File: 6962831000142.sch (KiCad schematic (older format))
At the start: 75 parts, among them J1 1042490810, J10 A2, J11 B1, J12 B2, J13 C1, J14 C2, J15 D1, J16 D2, J17 SolderPoint +, J18 SolderPoint -, J19 FastenerDrillingGNDREF, J20 FastenerDrilling, J8 1909763-1, J9 A1, Q1 SI2323DS, SW1 SW_Reed_Opener, U1 CC2640R2FRSMT, U2 ADP160AUJZ-2.3-R7, U3 CMKT5087TR, U4 CMKT5087TR, U5 CMKT5087TR, U6 PS09, Y1 TSX-322524.0000MF15X-AC3, Y2 32.768kHz, Y3 24 MHz

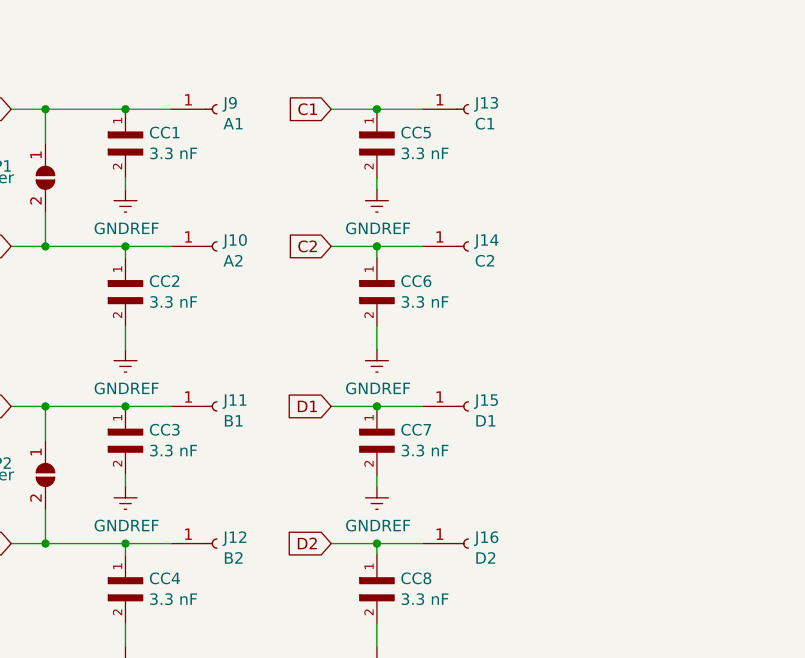
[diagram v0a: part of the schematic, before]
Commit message: se colocaron dos pads soldables
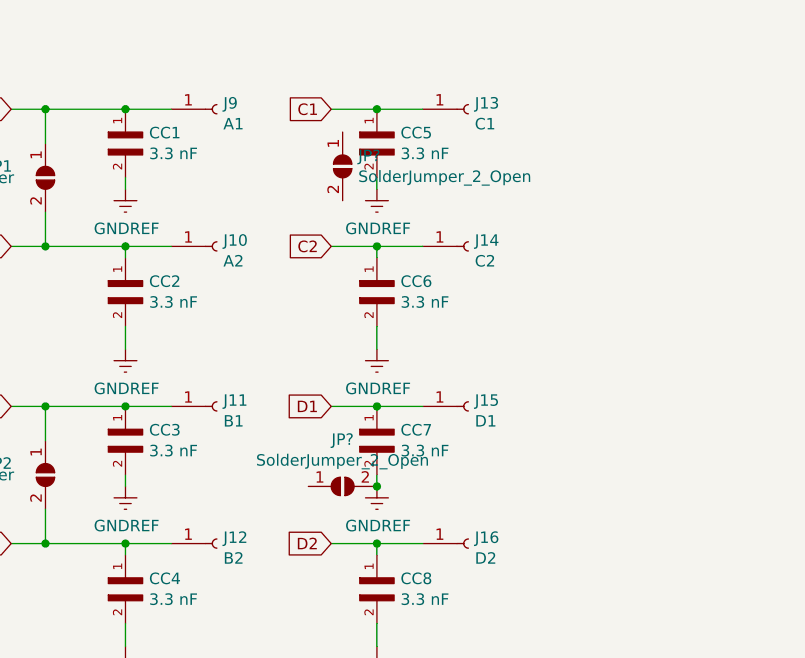
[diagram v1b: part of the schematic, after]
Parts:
- added JP? (x2): SolderJumper_2_Open, symbol Jumper:SolderJumper_2_Open
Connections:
- net GNDREF: now also JP?.2 (B)
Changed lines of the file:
@@
 Wire Wire Line
 	12700 3500 13050 3500
+$Comp
+L Jumper:SolderJumper_2_Open JP?
+U 1 1 5F74EED2
+P 14000 1850
+F 0 "JP?" V 13954 1918 50  0000 L CNN
+F 1 "SolderJumper_2_Open" V 14045 1918 50  0000 L CNN
+F 2 "" H 14000 1850 50  0001 C CNN
+F 3 "~" H 14000 1850 50  0001 C CNN
+	1    14000 1850
+	0    1    1    0
+$EndComp
+$Comp
+L Jumper:SolderJumper_2_Open JP?
+U 1 1 5F74F512
+P 14000 3250
+F 0 "JP?" H 14000 3455 50  0000 C CNN
+F 1 "SolderJumper_2_Open" H 14000 3364 50  0000 C CNN
+F 2 "" H 14000 3250 50  0001 C CNN
+F 3 "~" H 14000 3250 50  0001 C CNN
+	1    14000 3250
+	1    0    0    -1
+$EndComp
+Connection ~ 14150 3250
 $EndSCHEMATC
